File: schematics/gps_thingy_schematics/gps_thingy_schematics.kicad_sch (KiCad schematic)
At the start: 4 parts, among them J1 Conn_01x04, J2 Conn_01x01, J3 Conn_01x06, J4 Conn_01x04

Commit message: finishing schematics
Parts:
- added J5: Conn_01x11, symbol Connector_Generic:Conn_01x11
- added U1: RASPBERRY_PI_ZERO_2_W, RASPBERRY_PI_ZERO_2_W:MODULE_RASPBERRY_PI_ZERO_2_W, symbol rapi:RASPBERRY_PI_ZERO_2_W
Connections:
- net VIN is gone; now on net +3.3V: J3.1 (Pin_1)
- net +5V: now also U1.2 (5V_2)
- net GND: now also J5.11 (Pin_11), U1.6 (GND_6)
- net PPS: now also U1.12 (GPIO18/GPIO_GEN1)
- net SCL: now also U1.5 (GPIO3/SCL)
- net SDA: now also U1.3 (GPIO2/SDA1)
- net +3V renamed +3.3V
- net +3.3V: now also J5.10 (Pin_10), U1.1 (3V3_1)
- new net CS: J5.7 (Pin_7), U1.24 (GPIO8/SPI_~{CE0})
- new net MISO: J5.5 (Pin_5), U1.21 (GPIO9/SPI_MISO)
- new net MOSI: J5.6 (Pin_6), U1.19 (GPIO10/SPI_MOSI)
- new net SCK: J5.4 (Pin_4), U1.23 (GPIO11/SPI_SCLK)
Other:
- moved on the sheet: J1, J2, J3, J4

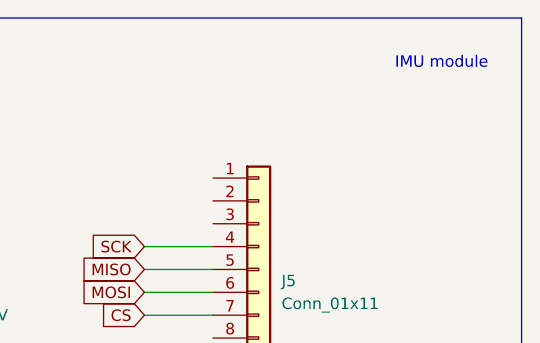
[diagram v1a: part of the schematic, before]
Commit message: add new 3d files and start writing firmware
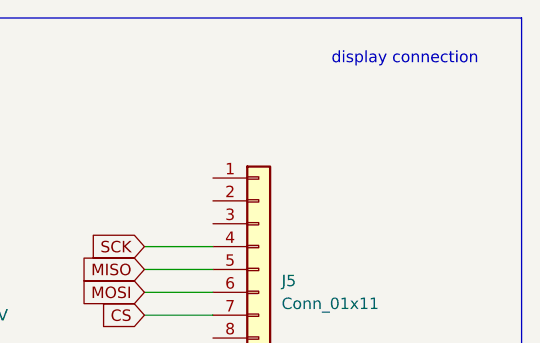
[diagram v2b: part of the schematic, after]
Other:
- note added: "display connection"
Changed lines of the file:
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@@
 		)
 	)
-	(text "IMU module"
+	(text "display connection"
 		(exclude_from_sim no)
-		(at 266.7 27.94 0)
+		(at 262.636 27.432 0)
 		(effects
 			(font
